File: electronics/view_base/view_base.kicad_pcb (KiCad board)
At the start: 2 copper layers, 81.2 x 81.2 mm, 107 parts, among them J1 BLDC, J2 USB_C_Receptacle_USB2.0, J3 LCD, J4 A, J5 B, Q1 MMBT4403, Q2 UMH3N, U1 MT6701-CT, U2 T-Micro32_Plus, U3 CH340C, U4 HX711, U5 TMC6300, U6 AP2114HA-3.3, U7 SN74LV1T34DBV, U8 VEML7700, U9 TS1117BCW33_RPG

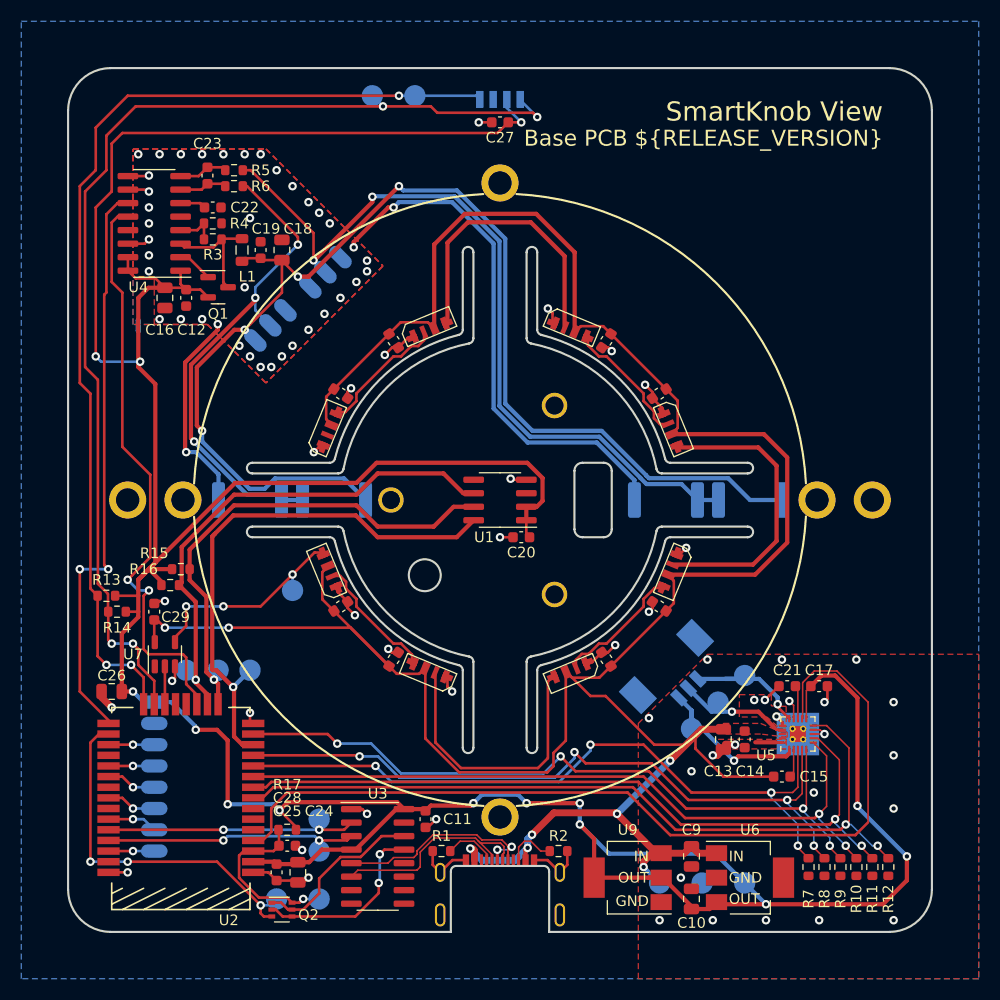
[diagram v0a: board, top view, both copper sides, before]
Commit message: Use ESP32-S3-MINI-1 in place of TMicro32 Plus
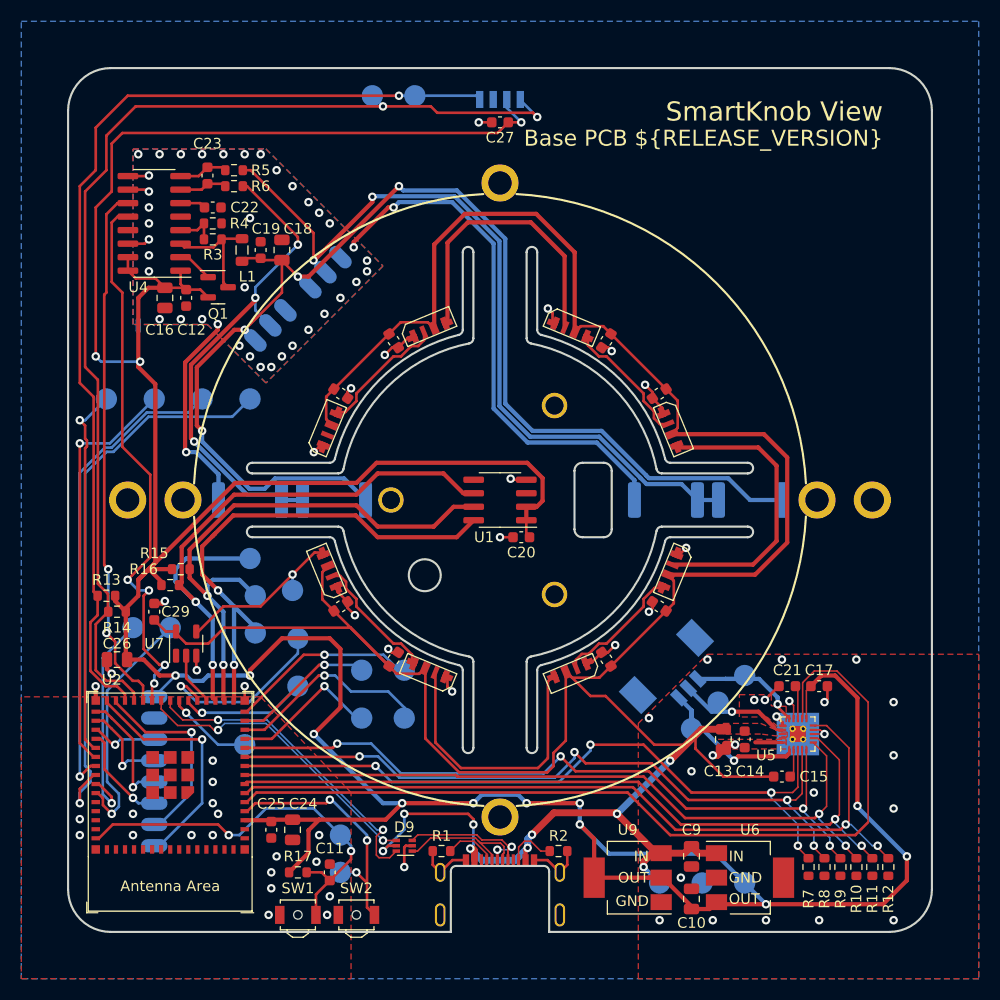
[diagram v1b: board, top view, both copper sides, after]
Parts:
- removed C28: 1uF, Capacitor_SMD:C_0603_1608Metric
- removed Q2: UMH3N, Package_TO_SOT_SMD:SOT-363_SC-70-6
- removed U3: CH340C, Package_SO:SOIC-16_3.9x9.9mm_P1.27mm
- added D9: NUF2042XV6T1G, Package_TO_SOT_SMD:SOT-563, F.Cu at (91.0, 132.5)
- added SW1: SW_Push, Button_Switch_SMD:SW_SPST_B3U-3000P-B, F.Cu at (81.0, 139.0)
- added SW2: SW_Push, Button_Switch_SMD:SW_SPST_B3U-3000P-B, F.Cu at (86.5, 139.0)
- added TP17: MTMS, Modified:TestPoint_Pad_D2.0mm_ValueSilk, B.Cu at (76.5, 90.5)
- added TP18: MTDI, Modified:TestPoint_Pad_D2.0mm_ValueSilk, B.Cu at (72.0, 90.5)
- added TP19: MTDO, Modified:TestPoint_Pad_D2.0mm_ValueSilk, B.Cu at (67.5, 90.5)
- added TP20: MTCK, Modified:TestPoint_Pad_D2.0mm_ValueSilk, B.Cu at (63.0, 90.5)
- added TP21: IO8, Modified:TestPoint_Pad_D2.0mm_ValueSilk, B.Cu at (87.0, 120.5)
- added TP22: IO9, Modified:TestPoint_Pad_D2.0mm_ValueSilk, B.Cu at (91.0, 120.5)
- added TP23: IO10, Modified:TestPoint_Pad_D2.0mm_ValueSilk, B.Cu at (87.0, 116.0)
- added TP24: IO11, Modified:TestPoint_Pad_D2.0mm_ValueSilk, B.Cu at (91.0, 116.0)
- added TP25: IO16, Modified:TestPoint_Pad_D2.0mm_ValueSilk, B.Cu at (81.0, 113.0)
- added TP26: IO17, Modified:TestPoint_Pad_D2.0mm_ValueSilk, B.Cu at (81.0, 117.5)
- added TP27: IO18, Modified:TestPoint_Pad_D2.0mm_ValueSilk, B.Cu at (76.0, 123.0)
- C11: value 0.1uF -> 1uF
- C24: value 10uF -> 22uF
- U2: value T-Micro32_Plus -> ESP32-S3-MINI-1; footprint lilygo_micro32:T-Micro32 -> PCM_Espressif:ESP32-S3-MINI-1
- moved TP15 27.3 mm to (65.5, 112.0), turned to 0 degrees
- moved TP16 22.8 mm to (69.0, 112.0), turned to 0 degrees
- moved TP11 12.1 mm to (76.5, 105.5), turned to -90 degrees
- moved U2 11.8 mm to (69.0, 125.8)
- moved C11 10.3 mm to (84.0, 135.0), turned to 90 degrees
- moved TP10 7.83 mm to (77.0, 109.0), turned to -90 degrees
- moved TP14 6.50 mm to (85.0, 135.0)
- moved TP13 6.32 mm to (85.0, 131.5)
- moved R17 4.12 mm to (81.0, 135.0), turned to 0 degrees
- moved C24 4.03 mm to (80.5, 131.0)
- moved C25 4.03 mm to (78.5, 131.0)
- moved TP9 3.54 mm to (77.0, 112.5), turned to -90 degrees
- moved C26 3.04 mm to (64.0, 115.0)
- moved U7 2.24 mm to (70.5, 113.5)
- moved J3 0.50 mm to (67.5, 118.5)
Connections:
- C11 pad 1: +3V3 -> /ESP32_EN
- TP15 pad 1: /USB_SERIAL_RXI -> /U0TXD
- TP16 pad 1: /USB_SERIAL_TXO -> /U0RXD
- U2 pad 10: /TMC_UL -> /TMC_VH
- U2 pad 11: /TMC_UH -> /TMC_WH
- U2 pad 12: /TMC_VH -> /IO8
- U2 pad 13: /MAG_CSN -> /IO9
- U2 pad 14: /TMC_WH -> /IO10
- U2 pad 15: GND -> /IO11
- U2 pad 16: /MAG_CLK -> /MAG_CSN
- U2 pad 17: /MAG_DO -> /MAG_CLK
- U2 pad 18: /STRAIN_DO -> /MAG_DO
- U2 pad 19: unconnected-(U2-Pad19) -> /LED_DATA_3V3
- U2 pad 2: +3V3 -> GND
- U2 pad 20: unconnected-(U2-Pad20) -> /IO16
- U2 pad 21: /LED_DATA_3V3 -> /IO17
- U2 pad 22: /SCL -> /IO18
- U2 pad 23: /SDA -> /MCU_USB_D-
- U2 pad 24: /STRAIN_SCK -> /MCU_USB_D+
- U2 pad 25: /ESP32_BOOT -> /STRAIN_DO
- U2 pad 26: /LCD_RST -> /STRAIN_SCK
- U2 pad 27: unconnected-(U2-Pad27) -> /SCL
- U2 pad 28: /LCD_SCK -> /SDA
- U2 pad 29: /LCD_DATA -> /LCD_CS
- U2 pad 3: /ESP32_EN -> +3V3
- U2 pad 30: unconnected-(U2-Pad30) -> /LCD_CMD
- U2 pad 31: /LCD_BACKLIGHT -> /LCD_DATA
- U2 pad 32: unconnected-(U2-Pad32) -> /LCD_SCK
- U2 pad 33: /LCD_CS -> /LCD_RST
- U2 pad 34: /USB_SERIAL_TXO -> /LCD_BACKLIGHT
- U2 pad 35: /USB_SERIAL_RXI -> /JTAG_MTCK
- U2 pad 36: /LCD_CMD -> /JTAG_MTDO
- U2 pad 37: unconnected-(U2-Pad37) -> /JTAG_MTDI
- U2 pad 38: GND -> /JTAG_MTMS
- U2 pad 4: /TMC_DIAG -> /ESP32_BOOT
- U2 pad 5: unconnected-(U2-Pad5) -> /TMC_DIAG
- U2 pad 6: unconnected-(U2-Pad6) -> /TMC_VL
- U2 pad 7: unconnected-(U2-Pad7) -> /TMC_WL
- U2 pad 8: /TMC_VL -> /TMC_UL
- U2 pad 9: /TMC_WL -> /TMC_UH
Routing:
- net /JTAG_MTMS: track 0.00 -> 53.4 mm, vias 0 -> 1
- net /JTAG_MTDI: track 0.00 -> 44.9 mm, vias 0 -> 1
- net /JTAG_MTDO: track 0.00 -> 38.9 mm, vias 0 -> 1
- net /JTAG_MTCK: track 0.00 -> 35.0 mm, vias 0 -> 1
- net /MCU_USB_D-: track 0.00 -> 30.3 mm, vias 0 -> 2
- net /MCU_USB_D+: track 0.00 -> 28.5 mm, vias 0 -> 2
- net /U0RXD: track 0.00 -> 23.5 mm, vias 0 -> 1
- net /USB_SERIAL_RXI: track 23.0 -> 0.00 mm, vias 2 -> 0
- net /USB_SERIAL_TXO: track 22.8 -> 0.00 mm, vias 2 -> 0
- net /ESP32_EN: track 15.4 -> 37.8 mm, vias 1 -> 2
- net /U0TXD: track 0.00 -> 20.6 mm, vias 0 -> 1
- net /IO9: track 0.00 -> 19.4 mm, vias 0 -> 1
- net /LCD_CMD: track 4.00 -> 22.7 mm
- net /IO11: track 0.00 -> 17.8 mm, vias 0 -> 1
- net /DTR: track 17.4 -> 0.00 mm, vias 2 -> 0
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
